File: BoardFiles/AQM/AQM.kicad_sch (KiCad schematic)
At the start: 40 parts, among them J1 Conn_01x04, J2 Conn_01x04, J3 Conn_01x04, J4 Conn_01x04, J5 Conn_01x04, U1 KB2040

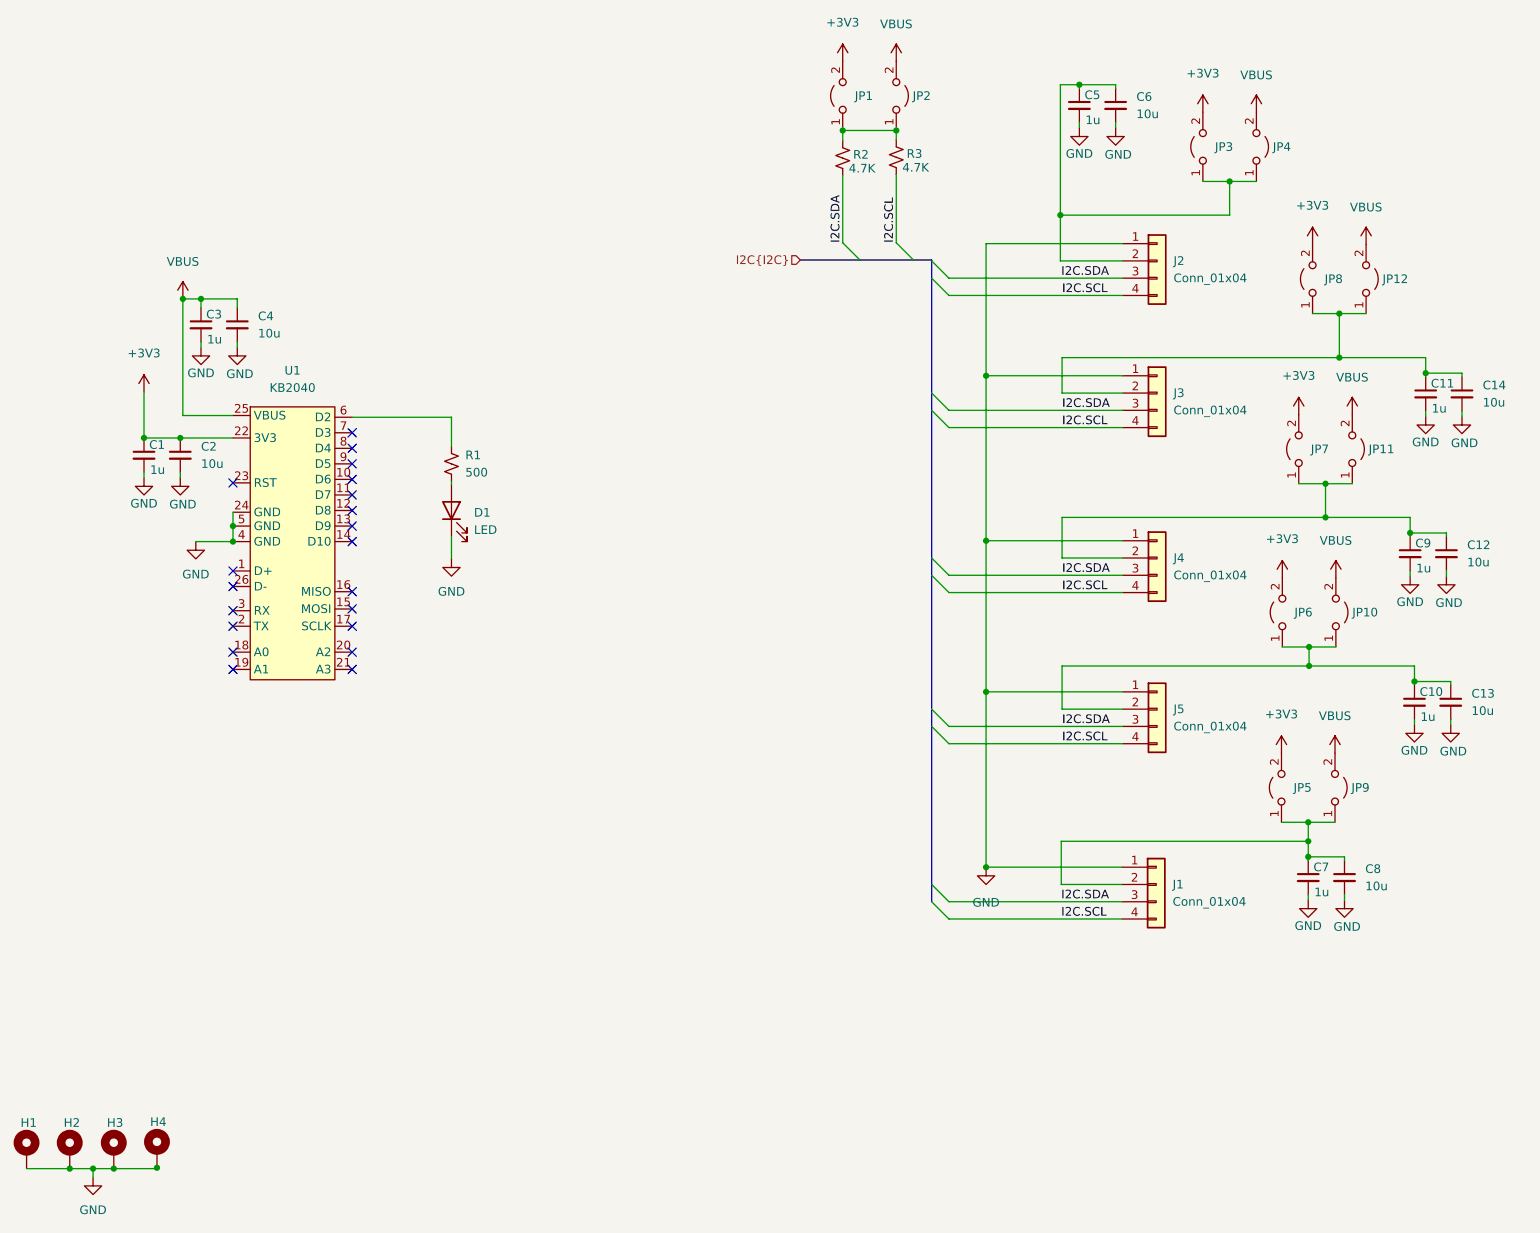
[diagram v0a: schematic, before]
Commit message: Redid copper to make it look pretty
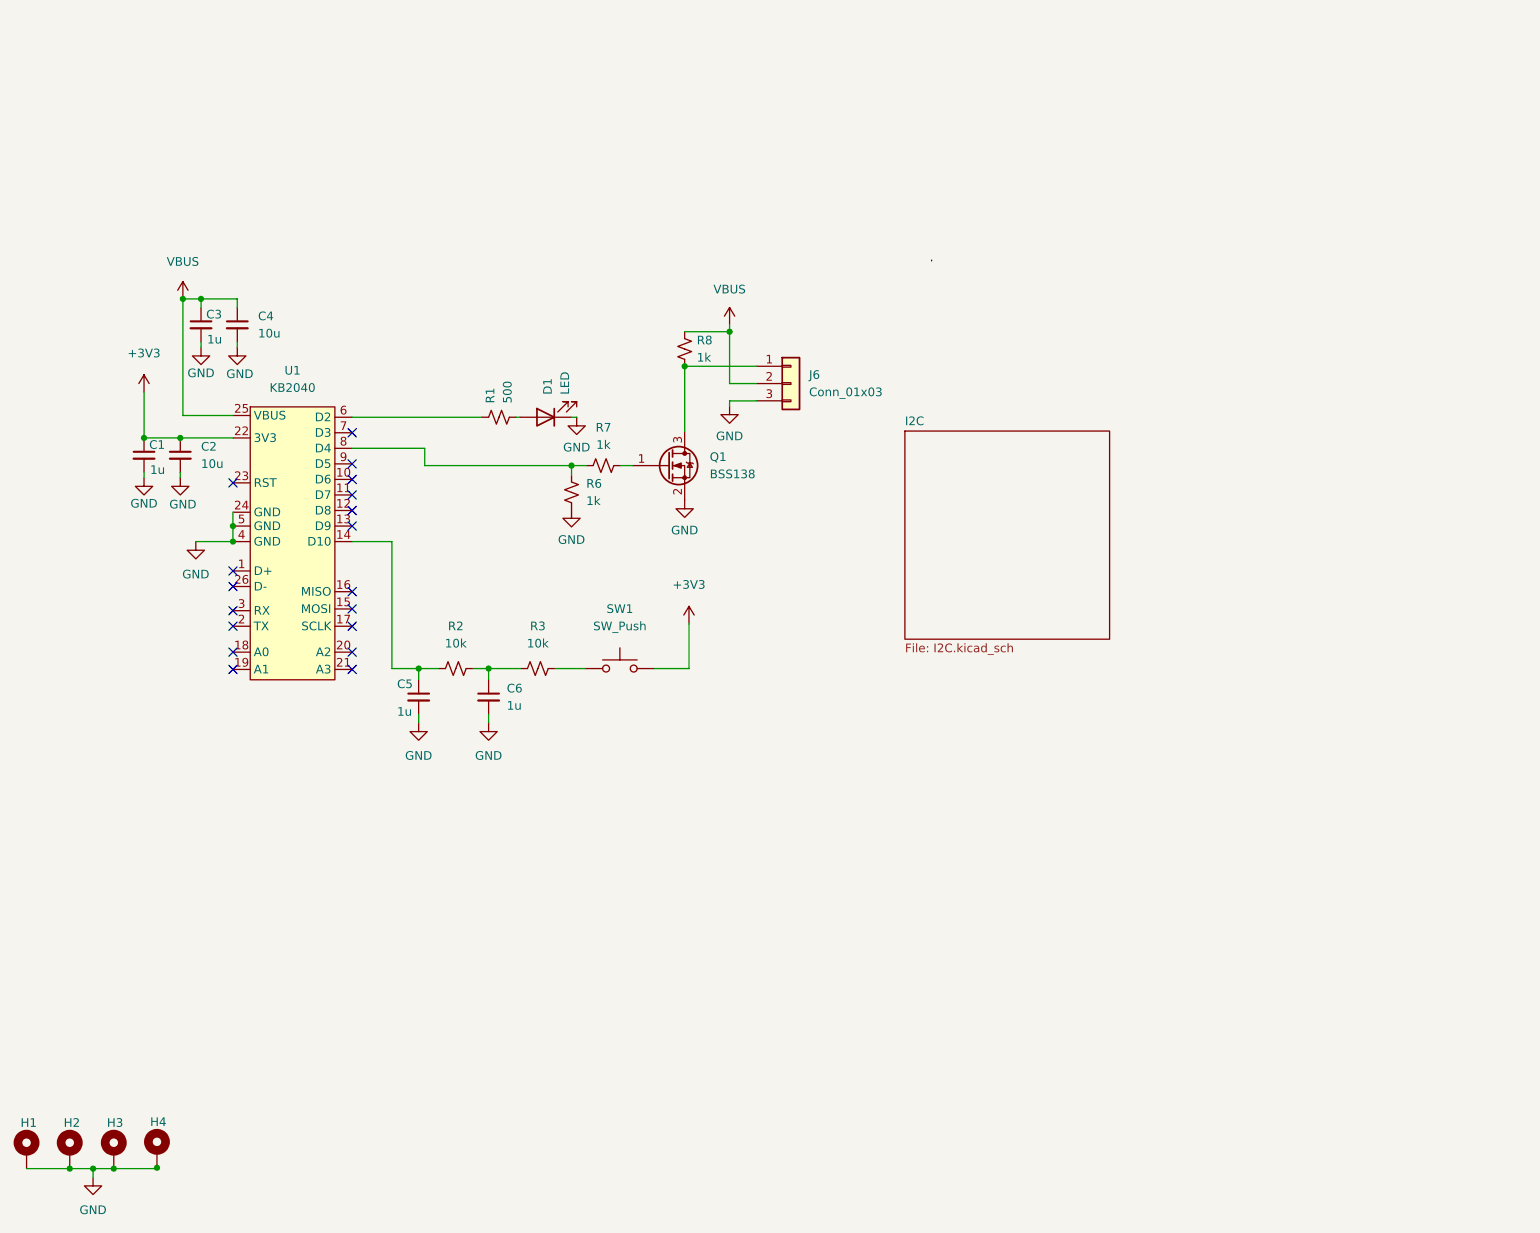
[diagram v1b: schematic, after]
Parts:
- removed C10, C11, C7, C9: 1u, Capacitor_SMD:C_0805_2012Metric, symbol Device:C_Small
- removed C12, C13, C14, C8: 10u, Capacitor_SMD:C_0805_2012Metric, symbol Device:C_Small
- removed J1, J2, J3, J4, J5: Conn_01x04, Connector_JST:JST_SH_BM04B-SRSS-TB_1x04-1MP_P1.00mm_Vertical, symbol Connector_Generic:Conn_01x04
- removed JP1, JP10, JP11, JP12, JP2, JP3, JP4, JP5, JP6, JP7, JP8, JP9: Jumper_2_Open, Jumper:SolderJumper-2_P1.3mm_Open_TrianglePad1.0x1.5mm, symbol Jumper:Jumper_2_Open
- added J6: Conn_01x03, Connector_PinHeader_2.54mm:PinHeader_1x03_P2.54mm_Vertical, symbol Connector_Generic:Conn_01x03
- added Q1: BSS138, Package_TO_SOT_SMD:SOT-23, symbol Transistor_FET:BSS138
- added R6, R7, R8: 1k, Resistor_SMD:R_0805_2012Metric, symbol Device:R_Small_US
- added SW1: SW_Push, Button_Switch_THT:SW_PUSH-12mm, symbol Switch:SW_Push
- C6: value 10u -> 1u
- R2, R3: value 4.7K -> 10k
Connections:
- net I2C.SDA is gone; now on an unnamed net: R2.2
- net +3V3: now also SW1.2
- net GND: now also J6.3 (Pin_3), Q1.2 (S), R6.1
- net VBUS: now also J6.2 (Pin_2), R8.2
- net at R3.1: now also C6.1; no longer R2.1
- net at C5.1: now also R2.1, U1.14 (D10); no longer C6.1
- net at U1.8 (D4): now also R6.2, R7.1
- net I2C.SCL: no longer names the net of R3.2
- net I2C.SCL: now also SW1.1
- new net: J6.1 (Pin_1), Q1.3 (D), R8.1
- new net: Q1.1 (G), R7.2
- no-connect marks 20 -> 18
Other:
- added sheet I2C (I2C.kicad_sch)
- moved on the sheet: D1, R1

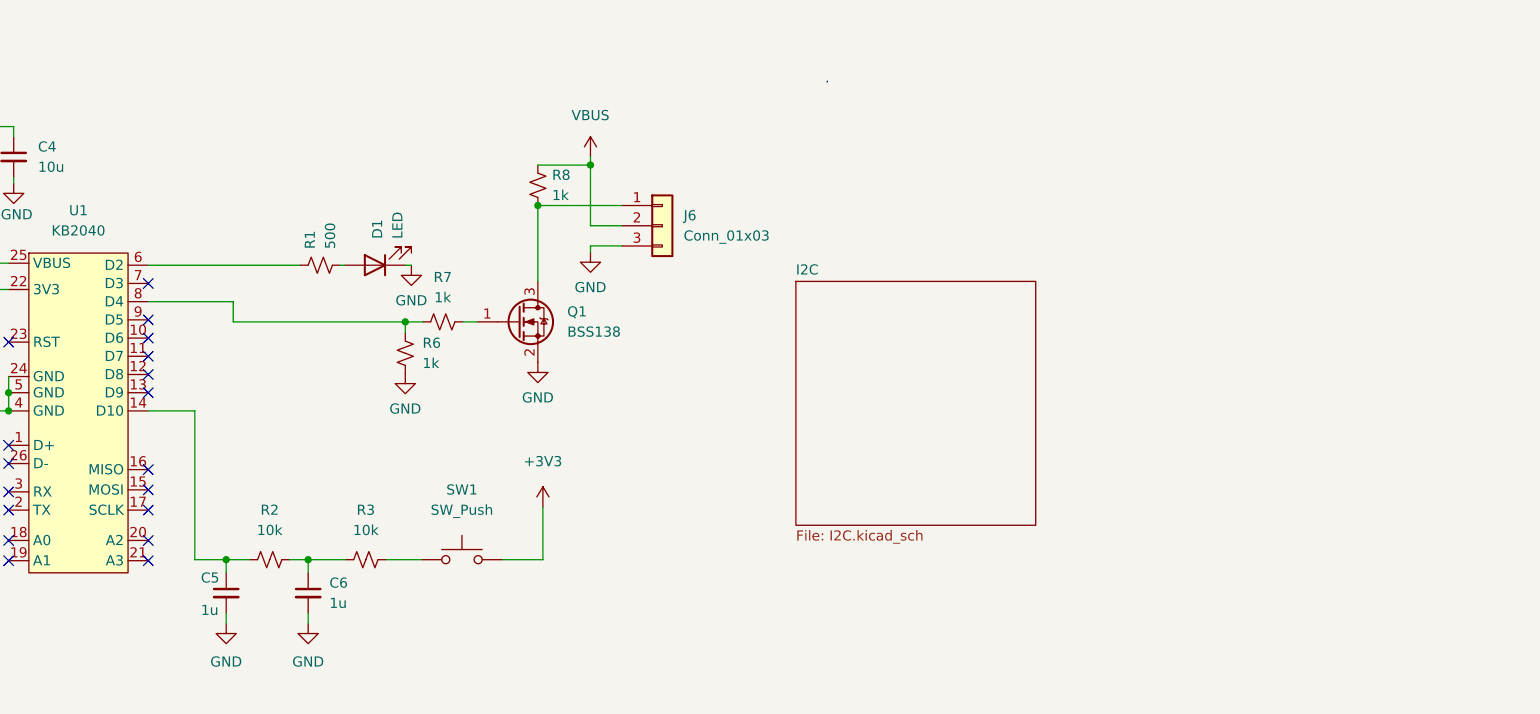
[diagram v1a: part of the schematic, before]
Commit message: Adding relative paths
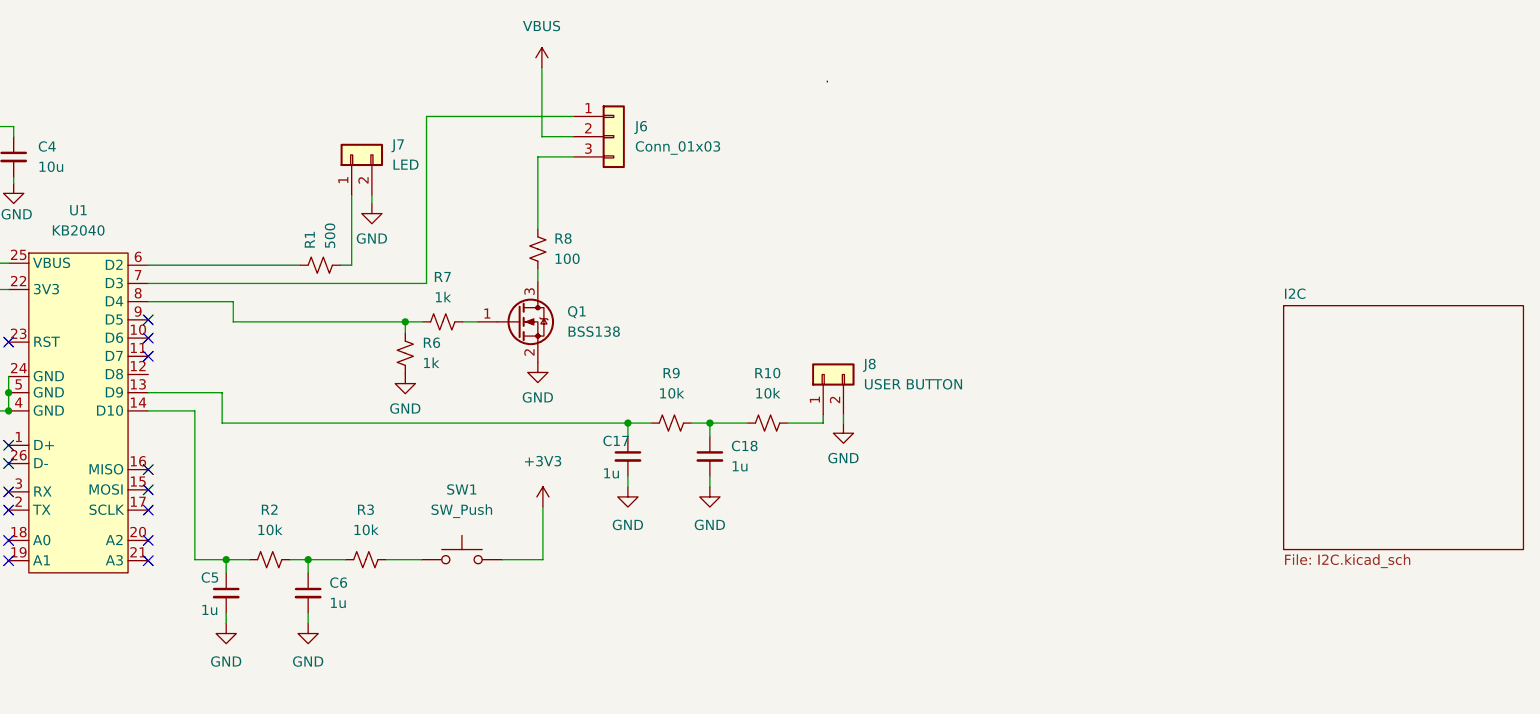
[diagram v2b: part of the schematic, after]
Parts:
- removed D1: LED, LED_THT:LED_D5.0mm_Clear, symbol Device:LED
- added C17, C18: 1u, Capacitor_SMD:C_0805_2012Metric, symbol Device:C_Small
- added J7: LED, Connector_PinSocket_2.54mm:PinSocket_1x02_P2.54mm_Vertical, symbol Connector_Generic:Conn_01x02
- added J8: USER BUTTON, Connector_PinSocket_2.54mm:PinSocket_1x02_P2.54mm_Vertical, symbol Connector_Generic:Conn_01x02
- added R10, R9: 10k, Resistor_SMD:R_0805_2012Metric, symbol Device:R_Small_US
- R8: value 1k -> 100
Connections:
- net GND: now also C17.2, C18.2, J7.2 (Pin_2), J8.2 (Pin_2); no longer J6.3 (Pin_3)
- net VBUS: no longer R8.2
- net at Q1.3 (D), R8.1: no longer J6.1 (Pin_1)
- net at R1.2: now also J7.1 (Pin_1)
- net at U1.13 (D9): now also C17.1, R9.1
- net at U1.7 (D3): now also J6.1 (Pin_1)
- new net: J6.3 (Pin_3), R8.2
- new net: C18.1, R10.1, R9.2
- new net: J8.1 (Pin_1), R10.2
- no-connect marks 18 -> 15
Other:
- moved on the sheet: J6, R8
